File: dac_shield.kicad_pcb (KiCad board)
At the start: 2 copper layers, 68.6 x 53.3 mm, 33 parts, among them P1 CONN_2, P2 CONN_2, P3 CONN_2, T1 VrefTest, U1 MCP4921, U2 TCA0372, U3 LM741

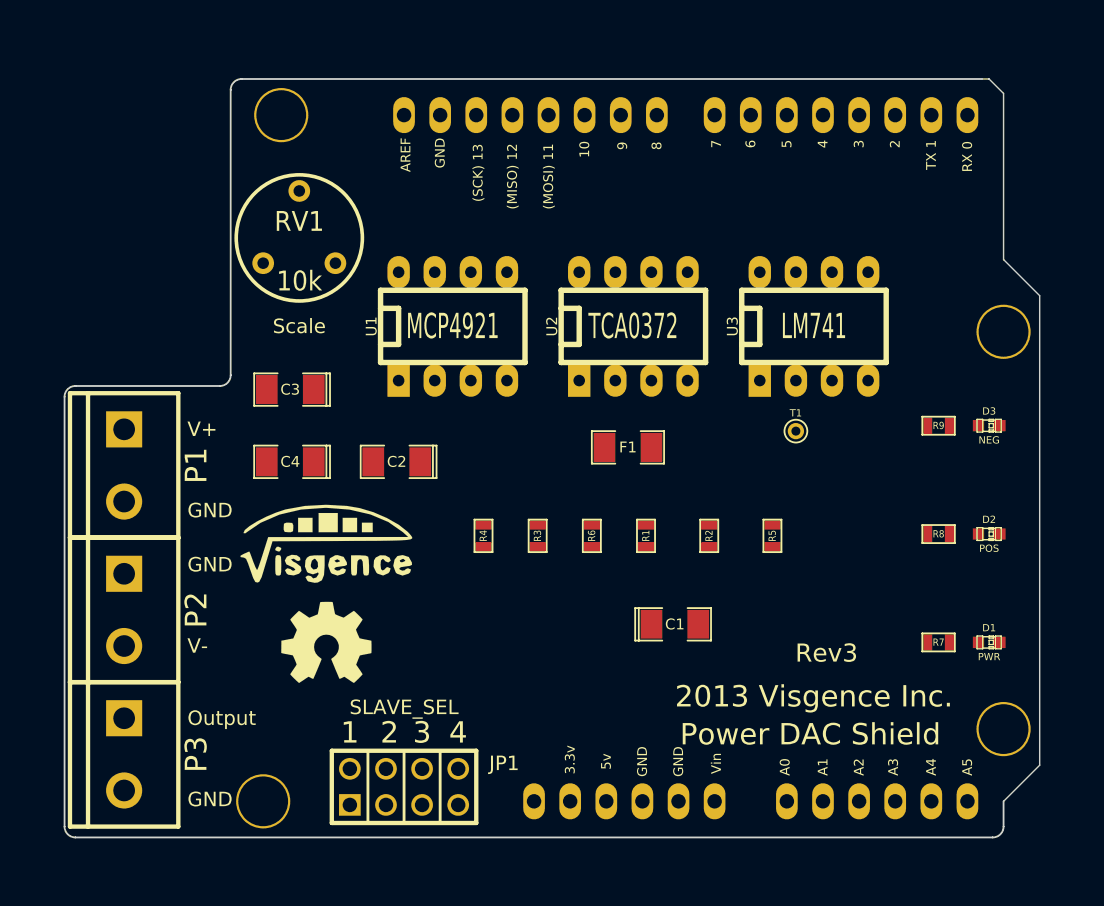
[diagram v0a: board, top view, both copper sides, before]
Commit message: Moved resistors to router easier
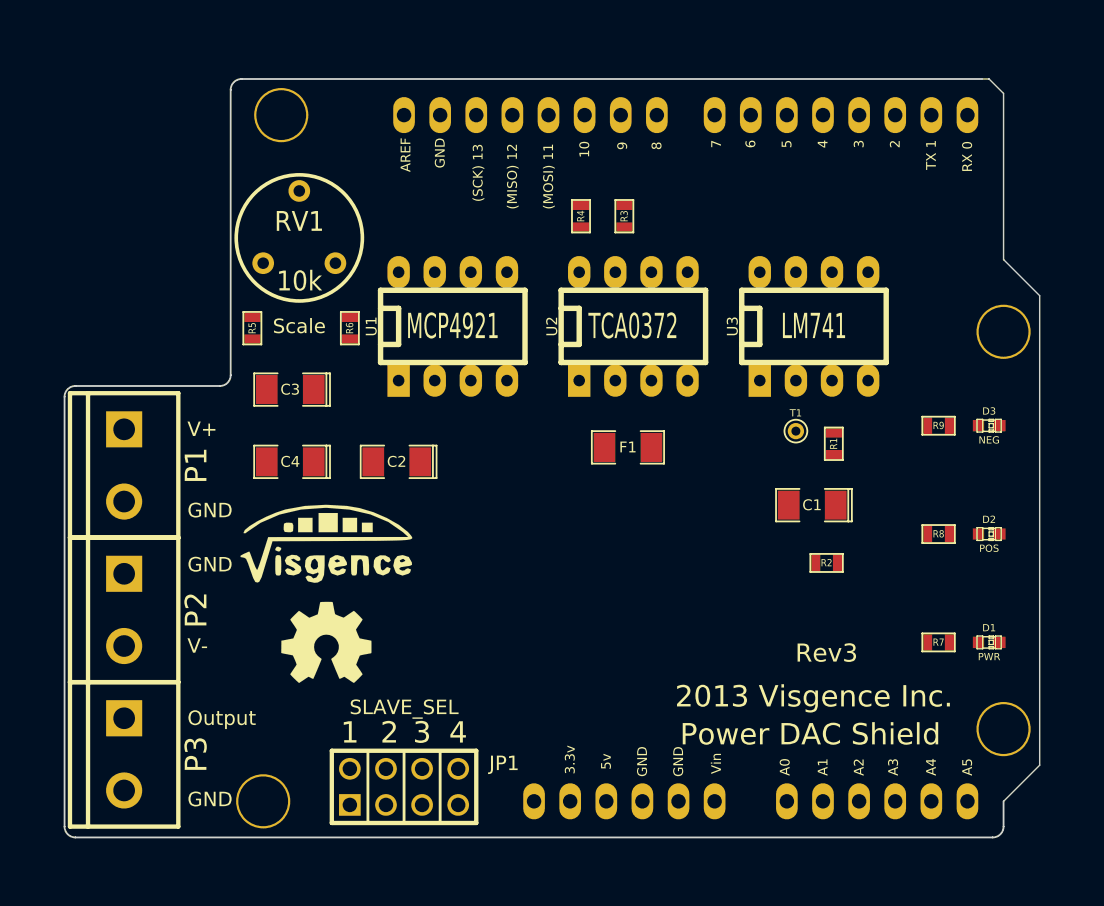
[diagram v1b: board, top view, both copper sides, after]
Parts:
- moved R5 39.4 mm to (43.7, 46.5)
- moved R4 23.5 mm to (66.8, 38.6)
- moved R3 23.3 mm to (69.8, 38.6)
- moved R6 22.4 mm to (50.5, 46.5), turned to 270 degrees
- moved R1 14.7 mm to (84.6, 54.6), turned to 270 degrees
- moved C1 12.8 mm to (83.1, 58.9), turned to 180 degrees
- moved R2 8.47 mm to (84.1, 63.0), turned to 0 degrees
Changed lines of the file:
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@@
     (links 59)
     (no_connects 59)
-    (area 30.429999 28.905999 99.110001 82.346001)
+    (area 29.972 28.448 99.568 83.566)
     (thickness 1.6)
     (drawings 61)
@@
   )
   (module SM0603 (layer F.Cu)
-    (at 59.944 61.087 90)
+    (at 66.802 38.608 90)
     (attr smd)
     (fp_text reference R4 (at 0 0 90) (layer F.SilkS)
@@
   )
   (module SM0603 (layer F.Cu)
-    (at 67.564 61.087 90)
-    (attr smd)
-    (fp_text reference R6 (at 0 0 90) (layer F.SilkS)
-      (effects (font (size 0.508 0.4572) (thickness 0.1143)))
-    )
-    (fp_text value 33k (at 0 0 90) (layer F.SilkS) hide
+    (at 50.546 46.482 270)
+    (attr smd)
+    (fp_text reference R6 (at 0 0 270) (layer F.SilkS)
+      (effects (font (size 0.508 0.4572) (thickness 0.1143)))
+    )
+    (fp_text value 33k (at 0 0 270) (layer F.SilkS) hide
+      (effects (font (size 0.508 0.4572) (thickness 0.1143)))
+    )
+    (fp_line (start -1.143 -0.635) (end 1.143 -0.635) (layer F.SilkS) (width 0.127))
+    (fp_line (start 1.143 -0.635) (end 1.143 0.635) (layer F.SilkS) (width 0.127))
+    (fp_line (start 1.143 0.635) (end -1.143 0.635) (layer F.SilkS) (width 0.127))
+    (fp_line (start -1.143 0.635) (end -1.143 -0.635) (layer F.SilkS) (width 0.127))
+    (pad 1 smd rect (at -0.762 0 270) (size 0.635 1.143)
+      (layers F.Cu F.Paste F.Mask)
+      (net 14 N-0000041)
+    )
+    (pad 2 smd rect (at 0.762 0 270) (size 0.635 1.143)
+      (layers F.Cu F.Paste F.Mask)
+      (net 20 N-000007)
+    )
+    (model smd\resistors\R0603.wrl
+      (at (xyz 0 0 0.001))
+      (scale (xyz 0.5 0.5 0.5))
+      (rotate (xyz 0 0 0))
+    )
+  )
+  (module SM0603 (layer F.Cu)
+    (at 43.688 46.482 90)
+    (attr smd)
+    (fp_text reference R5 (at 0 0 90) (layer F.SilkS)
+      (effects (font (size 0.508 0.4572) (thickness 0.1143)))
+    )
+    (fp_text value 12k (at 0 0 90) (layer F.SilkS) hide
       (effects (font (size 0.508 0.4572) (thickness 0.1143)))
     )
@@
     (pad 1 smd rect (at -0.762 0 90) (size 0.635 1.143)
       (layers F.Cu F.Paste F.Mask)
-      (net 14 N-0000041)
+      (net 4 GND)
     )
     (pad 2 smd rect (at 0.762 0 90) (size 0.635 1.143)
       (layers F.Cu F.Paste F.Mask)
-      (net 20 N-000007)
+      (net 13 N-0000040)
     )
     (model smd\resistors\R0603.wrl
@@
   )
   (module SM0603 (layer F.Cu)
-    (at 80.264 61.087 90)
-    (attr smd)
-    (fp_text reference R5 (at 0 0 90) (layer F.SilkS)
-      (effects (font (size 0.508 0.4572) (thickness 0.1143)))
-    )
-    (fp_text value 12k (at 0 0 90) (layer F.SilkS) hide
-      (effects (font (size 0.508 0.4572) (thickness 0.1143)))
-    )
-    (fp_line (start -1.143 -0.635) (end 1.143 -0.635) (layer F.SilkS) (width 0.127))
-    (fp_line (start 1.143 -0.635) (end 1.143 0.635) (layer F.SilkS) (width 0.127))
-    (fp_line (start 1.143 0.635) (end -1.143 0.635) (layer F.SilkS) (width 0.127))
-    (fp_line (start -1.143 0.635) (end -1.143 -0.635) (layer F.SilkS) (width 0.127))
-    (pad 1 smd rect (at -0.762 0 90) (size 0.635 1.143)
-      (layers F.Cu F.Paste F.Mask)
-      (net 4 GND)
-    )
-    (pad 2 smd rect (at 0.762 0 90) (size 0.635 1.143)
-      (layers F.Cu F.Paste F.Mask)
-      (net 13 N-0000040)
-    )
-    (model smd\resistors\R0603.wrl
-      (at (xyz 0 0 0.001))
-      (scale (xyz 0.5 0.5 0.5))
-      (rotate (xyz 0 0 0))
-    )
-  )
-  (module SM0603 (layer F.Cu)
-    (at 63.754 61.087 270)
+    (at 69.85 38.608 270)
     (attr smd)
     (fp_text reference R3 (at 0 0 270) (layer F.SilkS)
@@
   )
   (module SM0603 (layer F.Cu)
-    (at 71.374 61.087 90)
-    (attr smd)
-    (fp_text reference R1 (at 0 0 90) (layer F.SilkS)
-      (effects (font (size 0.508 0.4572) (thickness 0.1143)))
-    )
-    (fp_text value 22k (at 0 0 90) (layer F.SilkS) hide
+    (at 84.582 54.61 270)
+    (attr smd)
+    (fp_text reference R1 (at 0 0 270) (layer F.SilkS)
+      (effects (font (size 0.508 0.4572) (thickness 0.1143)))
+    )
+    (fp_text value 22k (at 0 0 270) (layer F.SilkS) hide
       (effects (font (size 0.508 0.4572) (thickness 0.1143)))
     )
@@
     (fp_line (start 1.143 0.635) (end -1.143 0.635) (layer F.SilkS) (width 0.127))
     (fp_line (start -1.143 0.635) (end -1.143 -0.635) (layer F.SilkS) (width 0.127))
-    (pad 1 smd rect (at -0.762 0 90) (size 0.635 1.143)
+    (pad 1 smd rect (at -0.762 0 270) (size 0.635 1.143)
       (layers F.Cu F.Paste F.Mask)
       (net 19 N-000006)
     )
-    (pad 2 smd rect (at 0.762 0 90) (size 0.635 1.143)
+    (pad 2 smd rect (at 0.762 0 270) (size 0.635 1.143)
       (layers F.Cu F.Paste F.Mask)
       (net 22 VDD)
@@
   )
   (module SM0603 (layer F.Cu)
-    (at 75.819 61.087 90)
-    (attr smd)
-    (fp_text reference R2 (at 0 0 90) (layer F.SilkS)
-      (effects (font (size 0.508 0.4572) (thickness 0.1143)))
-    )
-    (fp_text value 10k (at 0 0 90) (layer F.SilkS) hide
+    (at 84.074 62.992)
+    (attr smd)
+    (fp_text reference R2 (at 0 0) (layer F.SilkS)
+      (effects (font (size 0.508 0.4572) (thickness 0.1143)))
+    )
+    (fp_text value 10k (at 0 0) (layer F.SilkS) hide
       (effects (font (size 0.508 0.4572) (thickness 0.1143)))
     )
@@
     (fp_line (start 1.143 0.635) (end -1.143 0.635) (layer F.SilkS) (width 0.127))
     (fp_line (start -1.143 0.635) (end -1.143 -0.635) (layer F.SilkS) (width 0.127))
-    (pad 1 smd rect (at -0.762 0 90) (size 0.635 1.143)
-      (layers F.Cu F.Paste F.Mask)
-      (net 4 GND)
-    )
-    (pad 2 smd rect (at 0.762 0 90) (size 0.635 1.143)
+    (pad 1 smd rect (at -0.762 0) (size 0.635 1.143)
+      (layers F.Cu F.Paste F.Mask)
+      (net 4 GND)
+    )
+    (pad 2 smd rect (at 0.762 0) (size 0.635 1.143)
       (layers F.Cu F.Paste F.Mask)
       (net 19 N-000006)
@@
   )
   (module SM1206POL (layer F.Cu)
-    (at 73.406 67.31)
-    (attr smd)
-    (fp_text reference C1 (at 0 0) (layer F.SilkS)
+    (at 83.058 58.928 180)
+    (attr smd)
+    (fp_text reference C1 (at 0 0 180) (layer F.SilkS)
       (effects (font (size 0.762 0.762) (thickness 0.127)))
     )
-    (fp_text value 100n (at 0 0) (layer F.SilkS) hide
+    (fp_text value 100n (at 0 0 180) (layer F.SilkS) hide
       (effects (font (size 0.762 0.762) (thickness 0.127)))
     )
@@
     (fp_line (start 2.54 1.143) (end 0.889 1.143) (layer F.SilkS) (width 0.127))
     (fp_line (start -0.889 -1.143) (end -2.54 -1.143) (layer F.SilkS) (width 0.127))
-    (pad 1 smd rect (at -1.651 0) (size 1.524 2.032)
+    (pad 1 smd rect (at -1.651 0 180) (size 1.524 2.032)
       (layers F.Cu F.Paste F.Mask)
       (net 19 N-000006)
     )
-    (pad 2 smd rect (at 1.651 0) (size 1.524 2.032)
-      (layers F.Cu F.Paste F.Mask)
-      (net 4 GND)
+    (pad 2 smd rect (at 1.651 0 180) (size 1.524 2.032)
+      (layers F.Cu F.Paste F.Mask)
+      (net 4 GND)

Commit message: First route and fill
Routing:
- net GND: track 0.00 -> 178.9 mm, vias 0 -> 7
- net VDD: track 0.00 -> 86.2 mm, vias 0 -> 5
- net VSS: track 0.00 -> 78.8 mm, vias 0 -> 3
- net N-0000034: track 0.00 -> 70.3 mm, vias 0 -> 4
- net N-0000036: track 0.00 -> 66.7 mm, vias 0 -> 6
- net +5V: track 0.00 -> 63.4 mm, vias 0 -> 2
- net N-0000033: track 0.00 -> 60.4 mm, vias 0 -> 2
- net N-0000035: track 0.00 -> 60.3 mm, vias 0 -> 1
- net VREF: track 0.00 -> 46.6 mm, vias 0 -> 2
- net N-000009: track 0.00 -> 41.9 mm, vias 0 -> 1
- net N-0000037: track 0.00 -> 35.6 mm
- net N-0000044: track 0.00 -> 34.5 mm, vias 0 -> 1
- net N-000007: track 0.00 -> 28.6 mm, vias 0 -> 1
- net N-0000043: track 0.00 -> 24.1 mm, vias 0 -> 2
- net CLK: track 0.00 -> 21.9 mm
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- added copper zone on B.Cu, net GND
- added copper zone on F.Cu, net GND

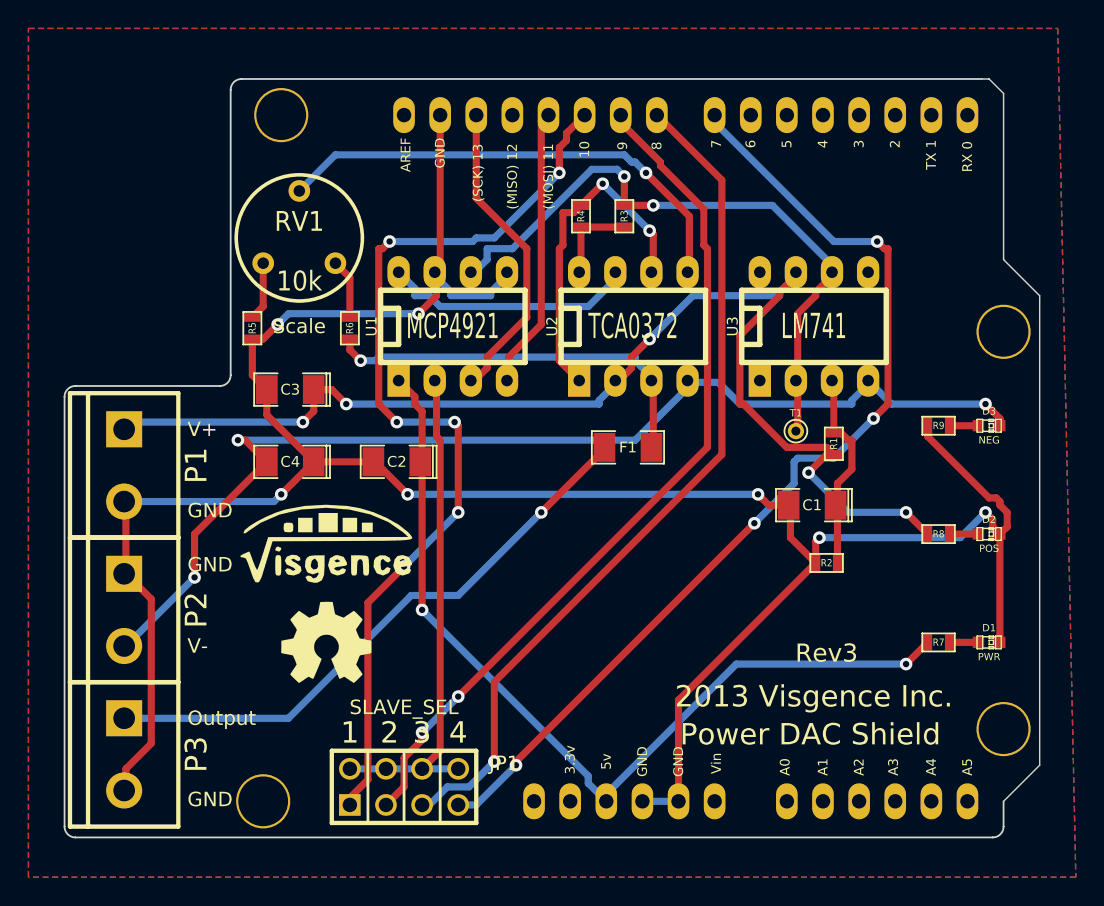
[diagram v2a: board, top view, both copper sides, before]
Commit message: Changed fuse package, rerouted
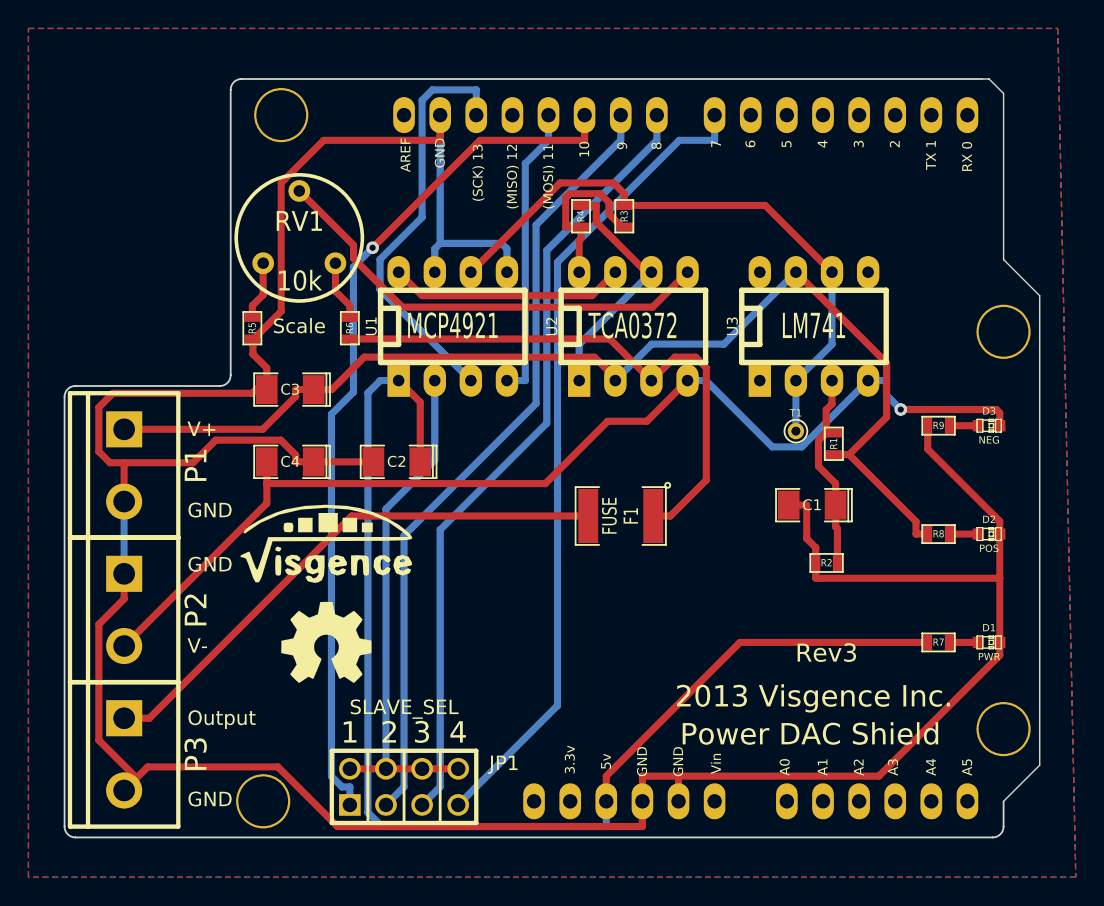
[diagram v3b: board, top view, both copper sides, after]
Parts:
- F1: footprint SM1206 -> SM1812
- moved F1 4.85 mm to (69.6, 59.7)
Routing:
- net GND: track 178.9 -> 219.4 mm, vias 7 -> 0
- net +5V: track 63.4 -> 85.6 mm, vias 2 -> 0
- net N-0000034: track 70.3 -> 57.4 mm, vias 4 -> 0
- net N-000007: track 28.6 -> 40.0 mm, vias 1 -> 0
- net CLK: track 21.9 -> 29.5 mm
- net N-0000043: track 24.1 -> 17.3 mm, vias 2 -> 0
- net VDD: track 86.2 -> 79.6 mm, vias 5 -> 0
- net N-0000036: track 66.7 -> 61.1 mm, vias 6 -> 1
- net N-0000042: track 6.53 -> 12.1 mm
- net N-0000033: track 60.4 -> 55.4 mm, vias 2 -> 0
- net N-0000035: track 60.3 -> 55.4 mm, vias 1 -> 0
- net N-000009: track 41.9 -> 38.5 mm, vias 1 -> 0
- net VREF: track 46.6 -> 43.3 mm, vias 2 -> 0
- net N-0000044: track 34.5 -> 32.3 mm, vias 1 -> 0
- net DAC_OUT: track 17.9 -> 16.6 mm
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
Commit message: Silkscreen updates and routed
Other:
- board text added: "2013 Visgence Inc Power DAC Shield www.visgence.com"
- board text added: "Reset"
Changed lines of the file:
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@@
     (area 27.94 25.4 101.600001 85.090001)
     (thickness 1.6)
-    (drawings 61)
+    (drawings 63)
     (tracks 218)
     (zones 0)
@@
       (effects (font (size 0.508 0.4572) (thickness 0.1143)))
     )
-    (fp_text value 33k (at 0 0 270) (layer F.SilkS) hide
+    (fp_text value 33k (at -0.127 1.016 270) (layer F.SilkS)
       (effects (font (size 0.508 0.4572) (thickness 0.1143)))
     )
@@
       (effects (font (size 0.508 0.4572) (thickness 0.1143)))
     )
-    (fp_text value 12k (at 0 0 90) (layer F.SilkS) hide
+    (fp_text value 12k (at 0.127 1.143 90) (layer F.SilkS)
       (effects (font (size 0.508 0.4572) (thickness 0.1143)))
     )
@@
       (effects (font (size 0.508 0.4572) (thickness 0.1143)))
     )
-    (fp_text value 22k (at 0 0 270) (layer F.SilkS) hide
+    (fp_text value 22k (at 0 -1.27 270) (layer F.SilkS)
       (effects (font (size 0.508 0.4572) (thickness 0.1143)))
     )
@@
       (effects (font (size 0.508 0.4572) (thickness 0.1143)))
     )
-    (fp_text value 10k (at 0 0) (layer F.SilkS) hide
+    (fp_text value 10k (at 0.127 1.27) (layer F.SilkS)
       (effects (font (size 0.508 0.4572) (thickness 0.1143)))
     )
@@
       (effects (font (size 0.762 0.762) (thickness 0.127)))
     )
-    (fp_text value 100n (at 0 0 180) (layer F.SilkS) hide
+    (fp_text value 100n (at 0 1.905 180) (layer F.SilkS)
       (effects (font (size 0.762 0.762) (thickness 0.127)))
     )
@@
       (effects (font (size 0.762 0.762) (thickness 0.127)))
     )
-    (fp_text value 47u (at 0 0 180) (layer F.SilkS) hide
+    (fp_text value 47u (at -0.127 1.778 180) (layer F.SilkS)
       (effects (font (size 0.762 0.762) (thickness 0.127)))
     )
@@
       (effects (font (size 0.762 0.762) (thickness 0.127)))
     )
-    (fp_text value 1u (at 0 0 180) (layer F.SilkS) hide
+    (fp_text value 1u (at 0 1.778 180) (layer F.SilkS)
       (effects (font (size 0.762 0.762) (thickness 0.127)))
     )
@@
       (effects (font (size 0.762 0.762) (thickness 0.127)))
     )
-    (fp_text value 1u (at 0 0 180) (layer F.SilkS) hide
+    (fp_text value 1u (at 0 1.778 180) (layer F.SilkS)
       (effects (font (size 0.762 0.762) (thickness 0.127)))
     )
@@
     )
   )
+  (gr_text Reset (at 63.5 76.581 90) (layer F.SilkS)
+    (effects (font (size 0.6858 0.6858) (thickness 0.127)))
+  )
+  (gr_text "2013 Visgence Inc\nPower DAC Shield\nwww.visgence.com" (at 68.453 63.754) (layer B.SilkS)
+    (effects (font (size 1.524 1.524) (thickness 0.254)) (justify mirror))
+  )
   (gr_line (start 95.758 82.296) (end 31.242 82.296) (angle 90) (layer Edge.Cuts) (width 0.127))
